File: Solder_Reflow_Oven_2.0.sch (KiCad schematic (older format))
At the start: 45 parts, among them J1 Conn_01x02_Male, J2 USB_B_Micro, J3 Conn_01x02_Male, J4 Conn_02x03_Top_Bottom, J5 Conn_01x02_Top_Bottom, J6 Conn_01x02_Male, J7 Conn_01x24_Male, Q1 2SD1805, SW1 SW_DIP_x01, U1 LM2940IMPX-10/NOPB, U2 MAX31855KASA, U3 RCLAMP0502A.TCT, U4 STM32L053R6T6, U5 CDBHD140L-G, U6 F24-100-C2, Y1 Crystal_GND24

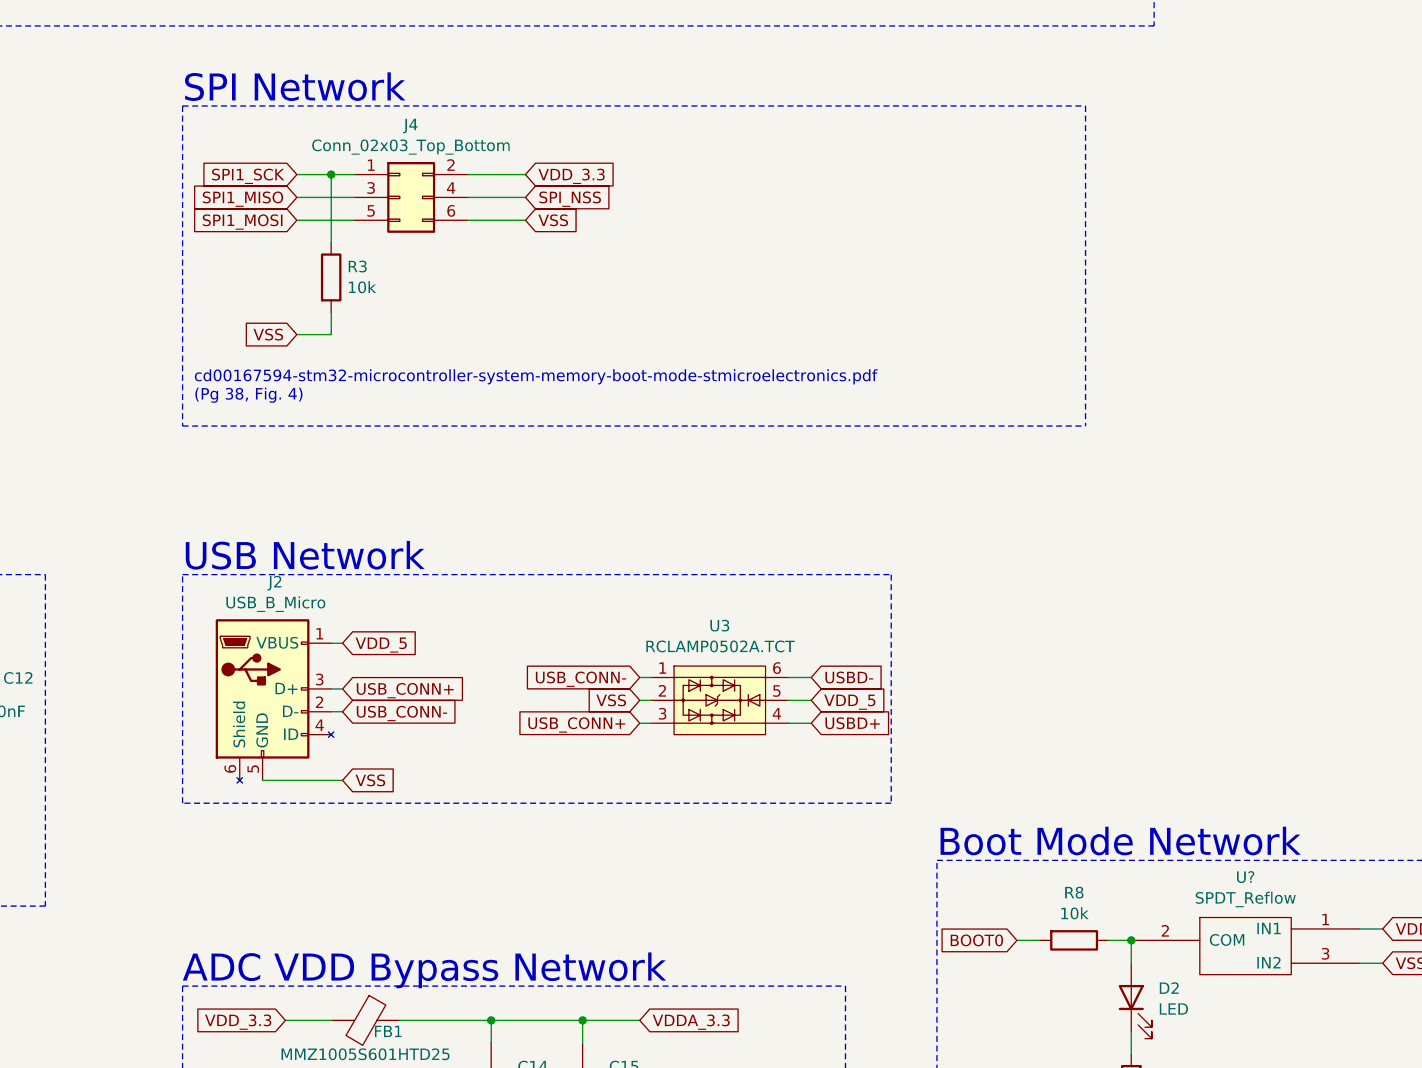
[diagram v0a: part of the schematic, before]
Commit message: Updating Design for through hole components
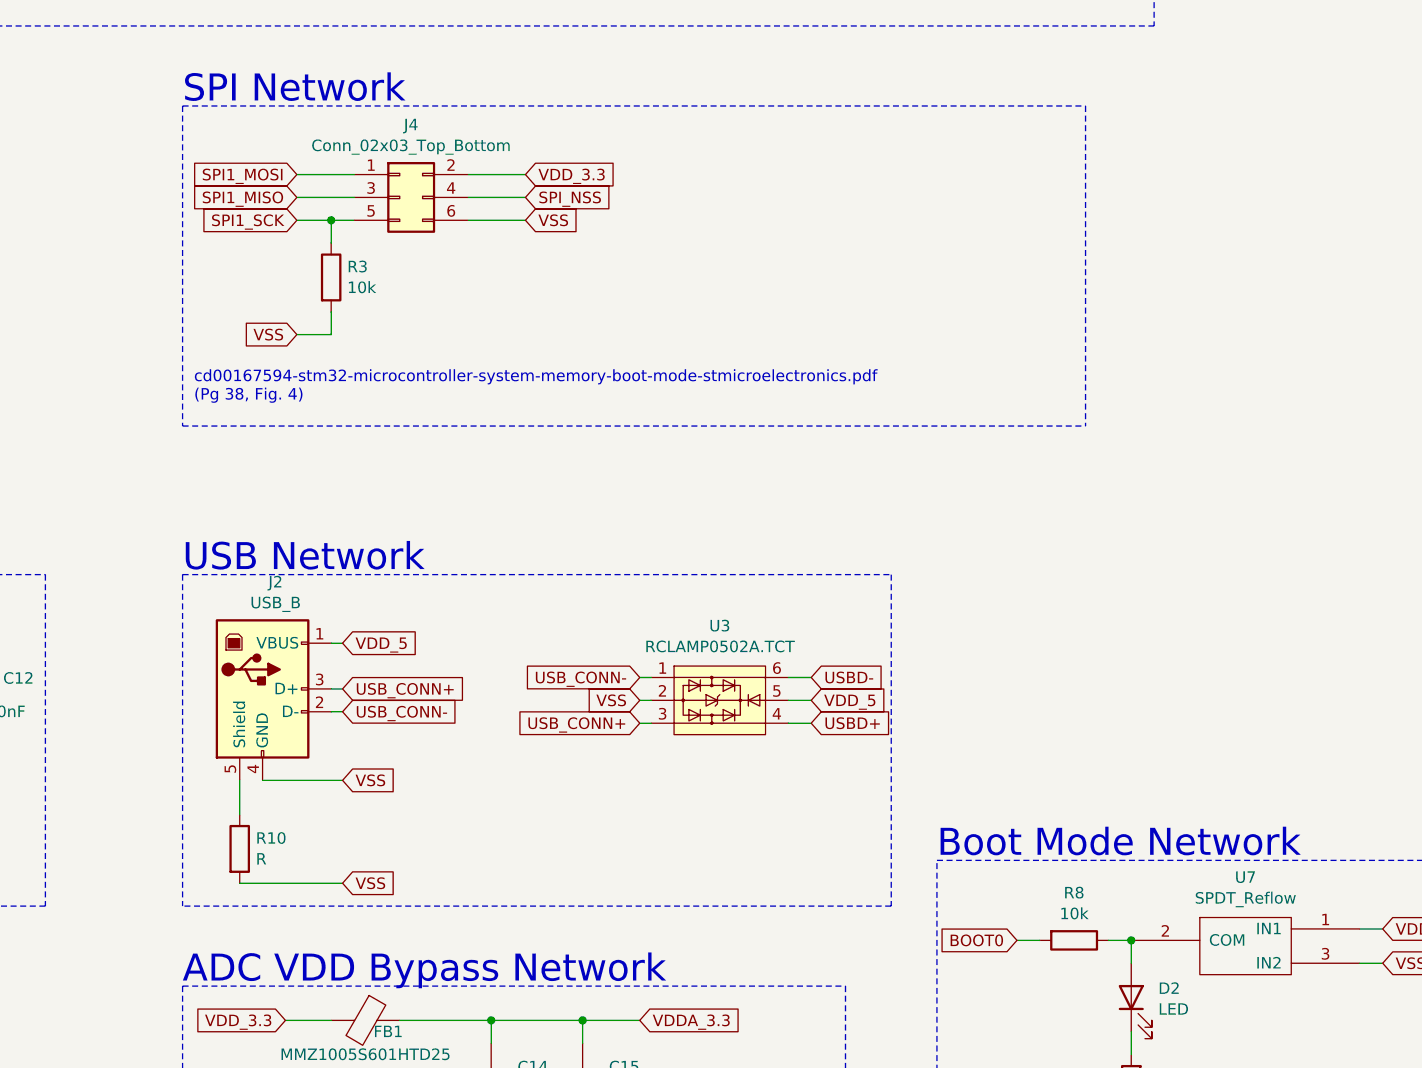
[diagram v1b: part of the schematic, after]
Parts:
- removed J2: USB_B_Micro, Connector_USB:USB_Micro-B_Molex-105017-0001, symbol micro_usb:USB_B_Micro
- added J2: USB_B, Connector_USB:USB_B_Lumberg_2411_02_Horizontal, symbol Connector:USB_B
- added R10: R, Resistor_SMD:R_0805_2012Metric_Pad1.20x1.40mm_HandSolder, symbol Device:R
- C1, C11, C12, C13, C14, C15, C16, C2, C3, C4, C5, C6, C7, C8, C9: footprint Capacitor_SMD:C_0603_1608Metric -> Capacitor_SMD:C_0805_2012Metric_Pad1.18x1.45mm_HandSolder
- C10: footprint Capacitor_SMD:C_0603_1608Metric -> Capacitor_THT:CP_Radial_D10.0mm_P7.50mm
- D1, D2: footprint LED_SMD:LED_0603_1608Metric_Pad1.05x0.95mm_HandSolder -> LED_SMD:LED_0805_2012Metric_Pad1.15x1.40mm_HandSolder
- FB1: footprint Inductor_SMD:L_0402_1005Metric_Pad0.77x0.64mm_HandSolder -> Inductor_SMD:L_0805_2012Metric_Pad1.15x1.40mm_HandSolder
- J4: footprint Connector_PinHeader_2.54mm:PinHeader_2x03_P2.54mm_Vertical_SMD -> Connector_PinHeader_2.54mm:PinHeader_2x03_P2.54mm_Vertical
- J5: footprint Connector_PinHeader_2.54mm:PinHeader_1x02_P2.54mm_Vertical_SMD_Pin1Left -> Connector_PinHeader_2.54mm:PinHeader_1x02_P2.54mm_Vertical
- R1, R2, R3, R4, R5, R6, R7, R8, R9: footprint Resistor_SMD:R_0603_1608Metric_Pad0.98x0.95mm_HandSolder -> Resistor_SMD:R_0805_2012Metric_Pad1.20x1.40mm_HandSolder
- U7: renamed from U?; footprint (none) -> SPDT:SPDT_Reflow
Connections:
- net SPI1_MOSI: now also J4.1 (Pin_1); no longer J4.5 (Pin_5)
- net SPI1_SCK: now also J4.5 (Pin_5); no longer J4.1 (Pin_1)
- net USB_CONN+: now also J2.3 (D+)
- net USB_CONN-: now also J2.2 (D-)
- net VDD_5: now also J2.1 (VBUS)
- net VSS: now also J2.4 (GND), R10.2
- new net: J2.5 (Shield), R10.1

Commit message: Updating board for version 2.0.0
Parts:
- removed R10: R, Resistor_SMD:R_0805_2012Metric_Pad1.20x1.40mm_HandSolder, symbol Device:R
- removed R5: 1k, Resistor_SMD:R_0805_2012Metric_Pad1.20x1.40mm_HandSolder, symbol Device:R
- added U8: LD1117S33TR_SOT223, Package_TO_SOT_SMD:SOT-223-3_TabPin2, symbol Regulator_Linear:LD1117S33TR_SOT223
- R4: value 2k -> 10
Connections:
- net VDD_10: now also U8.3 (VI); no longer R4.1
- net VDD_3.3: now also U8.2 (VO); no longer R4.2
- net VSS: now also R4.1, U8.1 (GND)
- net at U6.6 (S1_2): now also U5.4 (AC); no longer U6.7 (S2_1)
- net at U6.8 (S2_2): no longer U5.4 (AC)
- net at J2.5 (Shield): now also R4.2
- no-connect marks 2 -> 4
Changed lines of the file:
@@
 Wire Notes Line
 	5100 5100 8200 5100
-Wire Notes Line
-	8200 6550 5100 6550
 Text Notes 5100 5100 0    118  ~ 0
 USB Network
@@
 Wire Wire Line
 	6050 2050 6750 2050
-Text GLabel 7650 1700 2    50   Input ~ 0
+Text GLabel 7950 1700 2    50   Input ~ 0
 VDD_3.3
-Text GLabel 7650 2050 2    50   Input ~ 0
+Text GLabel 7950 2050 2    50   Input ~ 0
 VSS
 Connection ~ 6750 2050
-Wire Wire Line
-	7650 1350 7250 1350
 Connection ~ 6750 1350
-Text GLabel 7650 1350 2    50   Input ~ 0
+Text GLabel 7950 1350 2    50   Input ~ 0
 VDD_10
 $Comp
@@
 	1    0    0    -1
 $EndComp
-$Comp
-L Device:R R4
-U 1 1 61DC6952
-P 7250 1500
-F 0 "R4" H 7320 1546 50  0000 L CNN
-F 1 "2k" H 7320 1455 50  0000 L CNN
-F 2 "Resistor_SMD:R_0805_2012Metric_Pad1.20x1.40mm_HandSolder" V 7180 1500 50  0001 C CNN
-F 3 "~" H 7250 1500 50  0001 C CNN
-	1    7250 1500
-	1    0    0    -1
-$EndComp
-$Comp
-L Device:R R5
-U 1 1 61DC6F6E
-P 7250 1850
-F 0 "R5" H 7320 1896 50  0000 L CNN
-F 1 "1k" H 7320 1805 50  0000 L CNN
-F 2 "Resistor_SMD:R_0805_2012Metric_Pad1.20x1.40mm_HandSolder" V 7180 1850 50  0001 C CNN
-F 3 "~" H 7250 1850 50  0001 C CNN
-	1    7250 1850
-	1    0    0    -1
-$EndComp
-Connection ~ 7250 1350
-Wire Wire Line
-	7250 1350 6750 1350
-Wire Wire Line
-	6750 2050 7250 2050
-Wire Wire Line
-	7250 2000 7250 2050
-Connection ~ 7250 2050
-Wire Wire Line
-	7250 2050 7650 2050
-Wire Wire Line
-	7650 1700 7250 1700
-Wire Wire Line
-	7250 1700 7250 1650
-Connection ~ 7250 1700
 Wire Notes Line
 	800  2700 800  1000
@@
 Wire Wire Line
 	6850 9250 7000 9250
-$Comp
-L F24-100-C2:F24-100-C2 U6
-U 1 1 61AA4D6D
-P 1650 1550
-F 0 "U6" H 1725 1882 50  0000 C CNN
-F 1 "F24-100-C2" H 1725 1791 50  0000 C CNN
-F 2 "F24-100-C2:Transformer_Breve_TEZ-22x24" H 1650 1550 50  0001 C CNN
-F 3 "" H 1650 1550 50  0001 C CNN
-	1    1650 1550
-	1    0    0    -1
-$EndComp
 Wire Wire Line
 	1050 1650 1100 1650
@@
 	1050 2000 1050 2250
 Wire Wire Line
-	2350 2300 3300 2300
-Wire Wire Line
 	3300 1600 3600 1600
 Wire Wire Line
@@
 	3600 1700 3600 1850
 Wire Wire Line
-	3300 1600 3300 2300
-Wire Wire Line
-	2350 2000 2350 1900
+	3300 1600 3300 1900
 $Comp
 L Connector:Conn_01x24_Male J7
@@
 Wire Notes Line
 	8400 7900 10800 7900
-Wire Wire Line
-	5600 3350 5850 3350
-Wire Wire Line
-	5750 3650 5750 3550
-Connection ~ 5750 3550
-Wire Wire Line
-	5750 3550 5850 3550
-Wire Notes Line
-	5100 5100 5100 6550
-Wire Notes Line
-	8200 5100 8200 6550
+$Comp
+L Regulator_Linear:LD1117S33TR_SOT223 U8
+U 1 1 61C80020
+P 7550 1700
+F 0 "U8" H 7550 1942 50  0000 C CNN
+F 1 "LD1117S33TR_SOT223" H 7550 1851 50  0000 C CNN
+F 2 "Package_TO_SOT_SMD:SOT-223-3_TabPin2" H 7550 1900 50  0001 C CNN
+F 3 "http://www.st.com/st-web-ui/static/active/en/resource/technical/document/datasheet/CD00000544.pdf" H 7650 1450 50  0001 C CNN
+	1    7550 1700
+	1    0    0    -1
+$EndComp
+Wire Wire Line
+	6750 2050 7550 2050
+Wire Wire Line
+	7550 2000 7550 2050
+Connection ~ 7550 2050
+Wire Wire Line
+	7550 2050 7950 2050
+Wire Wire Line
+	7950 1700 7850 1700
+Wire Wire Line
+	6750 1350 7150 1350
+Wire Wire Line
+	7250 1700 7150 1700
+Wire Wire Line
+	7150 1700 7150 1350
+Connection ~ 7150 1350
+Wire Wire Line
+	7150 1350 7950 1350
 $Comp
 L Connector:USB_B J2
-U 1 1 61BFAA57
+U 1 1 61D0D3AA
 P 5450 5600
 F 0 "J2" H 5507 6067 50  0000 C CNN
@@
 $EndComp
 $Comp
-L Device:R R10
-U 1 1 61C39CC1
-P 5350 6300
-F 0 "R10" H 5420 6346 50  0000 L CNN
-F 1 "R" H 5420 6255 50  0000 L CNN
-F 2 "Resistor_SMD:R_0805_2012Metric_Pad1.20x1.40mm_HandSolder" V 5280 6300 50  0001 C CNN
-F 3 "~" H 5350 6300 50  0001 C CNN
-	1    5350 6300
-	1    0    0    -1
-$EndComp
-Text GLabel 5800 6450 2    50   Input ~ 0
-VSS
-Wire Wire Line
-	5350 6150 5350 6000
-Wire Wire Line
-	5350 6450 5800 6450
+L Device:R R4
+U 1 1 61D10C94
+P 5600 6250
+F 0 "R4" V 5393 6250 50  0000 C CNN
+F 1 "10" V 5484 6250 50  0000 C CNN
+F 2 "Resistor_SMD:R_0805_2012Metric_Pad1.20x1.40mm_HandSolder" V 5530 6250 50  0001 C CNN
+F 3 "~" H 5600 6250 50  0001 C CNN
+	1    5600 6250
+	0    1    1    0
+$EndComp
+Text GLabel 5800 6250 2    50   Input ~ 0
+VSS
+Wire Wire Line
+	5350 6000 5350 6250
+Wire Wire Line
+	5350 6250 5450 6250
+Wire Wire Line
+	5800 6250 5750 6250
+Wire Notes Line
+	5100 6400 8200 6400
+Wire Notes Line
+	8200 5100 8200 6400
+Wire Notes Line
+	5100 5100 5100 6400
+$Comp
+L F24-100-C2:F24-100-C2 U6
+U 1 1 61AA4D6D
+P 1650 1550
+F 0 "U6" H 1725 1882 50  0000 C CNN
+F 1 "F24-100-C2" H 1725 1791 50  0000 C CNN
+F 2 "F24-100-C2:Transformer_Breve_TEZ-22x24" H 1650 1550 50  0001 C CNN
+F 3 "" H 1650 1550 50  0001 C CNN
+	1    1650 1550
+	1    0    0    -1
+$EndComp
+Wire Wire Line
+	2350 1900 3300 1900
+NoConn ~ 2350 2000
+NoConn ~ 2350 2300
+Wire Wire Line
+	5600 3350 5850 3350
+Wire Wire Line
+	5750 3650 5750 3550
+Connection ~ 5750 3550
+Wire Wire Line
+	5750 3550 5850 3550
 $EndSCHEMATC
